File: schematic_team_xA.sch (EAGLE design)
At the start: 13 parts, among them U1 ATMEGA328P-AU

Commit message: Deleted copies
Deleted copies from the original location of the library files
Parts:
- removed R5, R6: (no value), resistor:R-US_R0402
- added R_VD1, R_VD2: 100kΩ, rcl:R-US_R0603
- C1: value (none) -> 100μF
- R_LED1, R_LED2, R_LED3, R_LED4: value (none) -> 150Ω
- renumbered R1 to R_LED1, R2 to R_LED2, R3 to R_LED3, R4 to R_LED4
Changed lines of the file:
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@@
 <part name="U1" library="ATMEGA328P-AU" deviceset="ATMEGA328P-AU" device=""/>
 <part name="U$1" library="nrf24l01" deviceset="NRF24L01" device=""/>
-<part name="R1" library="rcl" deviceset="R-US_" device="R0603"/>
-<part name="R2" library="rcl" deviceset="R-US_" device="R0603"/>
-<part name="R3" library="rcl" deviceset="R-US_" device="R0603"/>
-<part name="R4" library="rcl" deviceset="R-US_" device="R0603"/>
+<part name="R_LED1" library="rcl" deviceset="R-US_" device="R0603" value="150Ω"/>
+<part name="R_LED2" library="rcl" deviceset="R-US_" device="R0603" value="150Ω"/>
+<part name="R_LED3" library="rcl" deviceset="R-US_" device="R0603" value="150Ω"/>
+<part name="R_LED4" library="rcl" deviceset="R-US_" device="R0603" value="150Ω"/>
 <part name="D1" library="LEDs" deviceset="LED-RED" device="0603" value="RED"/>
 <part name="D2" library="LEDs" deviceset="LED-GREEN" device="0603" value="GREEN"/>
 <part name="D3" library="LEDs" deviceset="LED-GREEN" device="0603" value="GREEN"/>
 <part name="D4" library="LEDs" deviceset="LED-RED" device="0603" value="RED"/>
-<part name="C1" library="resistor" library_urn="urn:adsk.eagle:library:348" deviceset="C-US" device="C0805" package3d_urn="urn:adsk.eagle:package:26137/1"/>
-<part name="R5" library="resistor" deviceset="R-US_" device="R0402"/>
-<part name="R6" library="resistor" deviceset="R-US_" device="R0402"/>
+<part name="C1" library="resistor" library_urn="urn:adsk.eagle:library:348" deviceset="C-US" device="C0805" package3d_urn="urn:adsk.eagle:package:26137/1" value="100μF"/>
+<part name="R_VD1" library="rcl" deviceset="R-US_" device="R0603" value="100kΩ"/>
+<part name="R_VD2" library="rcl" deviceset="R-US_" device="R0603" value="100kΩ"/>
 </parts>
 <sheets>
@@
 <instance part="U1" gate="A" x="12.7" y="50.8"/>
 <instance part="U$1" gate="G$1" x="-7.62" y="58.42"/>
-<instance part="R1" gate="G$1" x="25.4" y="81.28"/>
-<instance part="R2" gate="G$1" x="25.4" y="73.66"/>
-<instance part="R3" gate="G$1" x="40.64" y="81.28"/>
-<instance part="R4" gate="G$1" x="40.64" y="73.66"/>
+<instance part="R_LED1" gate="G$1" x="25.4" y="81.28"/>
+<instance part="R_LED2" gate="G$1" x="25.4" y="73.66"/>
+<instance part="R_LED3" gate="G$1" x="40.64" y="81.28"/>
+<instance part="R_LED4" gate="G$1" x="40.64" y="73.66"/>
 <instance part="D1" gate="G$1" x="68.58" y="81.28"/>
 <instance part="D2" gate="G$1" x="81.28" y="81.28"/>
@@
 <instance part="D4" gate="G$1" x="68.58" y="71.12"/>
 <instance part="C1" gate="G$1" x="93.98" y="81.28"/>
-<instance part="R5" gate="G$1" x="53.34" y="81.28"/>
-<instance part="R6" gate="G$1" x="53.34" y="73.66"/>
+<instance part="R_VD1" gate="G$1" x="53.34" y="81.28"/>
+<instance part="R_VD2" gate="G$1" x="53.34" y="73.66"/>
 </instances>
 <busses>

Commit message: Added parts
Added parts to schematic
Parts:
- added U$2: TI-LM2665M6, TI-LM2665M6:TI-LM2665M6
- added U2: MPU-6050, MPU-6050:MPU-6050
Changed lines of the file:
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@@
 <part name="R_VD1" library="rcl" deviceset="R-US_" device="R0603" value="100kΩ"/>
 <part name="R_VD2" library="rcl" deviceset="R-US_" device="R0603" value="100kΩ"/>
+<part name="U$2" library="TI-LM2665M6" deviceset="TI-LM2665" device="M6"/>
+<part name="U2" library="MPU-6050" deviceset="MPU-6050" device=""/>
 </parts>
 <sheets>
@@
 <instance part="R_VD1" gate="G$1" x="53.34" y="81.28"/>
 <instance part="R_VD2" gate="G$1" x="53.34" y="73.66"/>
+<instance part="U$2" gate="G$1" x="-12.7" y="15.24"/>
+<instance part="U2" gate="G$1" x="132.08" y="78.74"/>
 </instances>
 <busses>

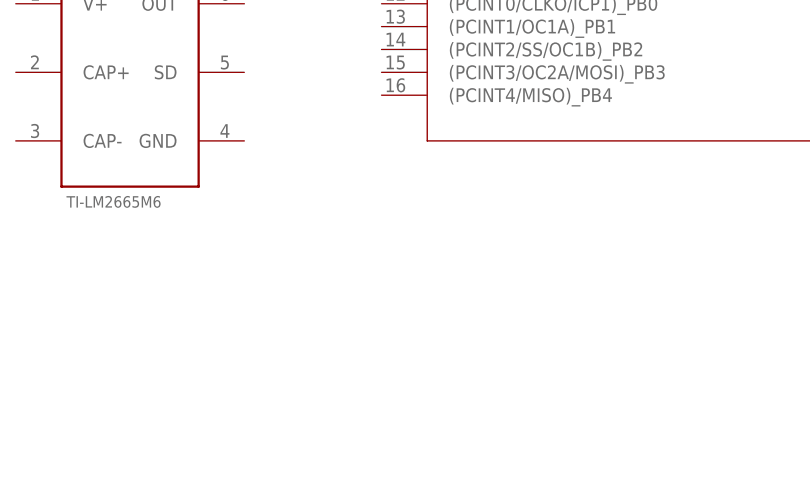
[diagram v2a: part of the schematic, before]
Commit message: NMOS Library
Created the NMOS library w/Rob and added it to the schematic
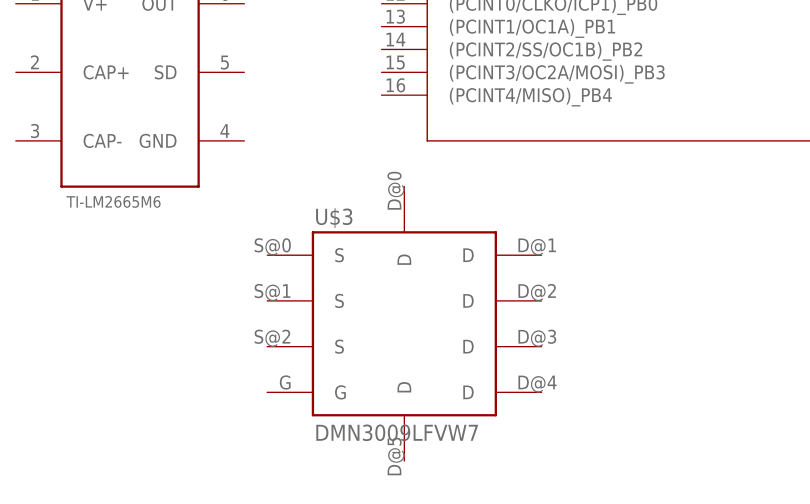
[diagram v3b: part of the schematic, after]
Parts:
- added U$3: DMN3009LFVW7, DMN3009LFVW:DMN3009LFVW7
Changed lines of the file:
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@@
 <part name="U$2" library="TI-LM2665M6" deviceset="TI-LM2665" device="M6"/>
 <part name="U2" library="MPU-6050" deviceset="MPU-6050" device=""/>
+<part name="U$3" library="DMN3009LFVW" deviceset="DMN3009LFVW" device="7"/>
 </parts>
 <sheets>
@@
 <instance part="U$2" gate="G$1" x="-12.7" y="15.24"/>
 <instance part="U2" gate="G$1" x="132.08" y="78.74"/>
+<instance part="U$3" gate="G$1" x="17.78" y="-12.7"/>
 </instances>
 <busses>

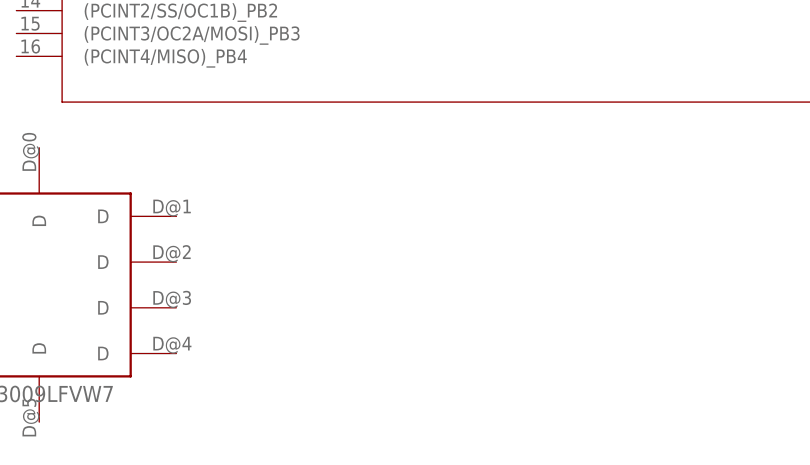
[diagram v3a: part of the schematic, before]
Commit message: Oscillator symbol/footprint
Created library file for our 16MHz oscillator and added it to the schematic
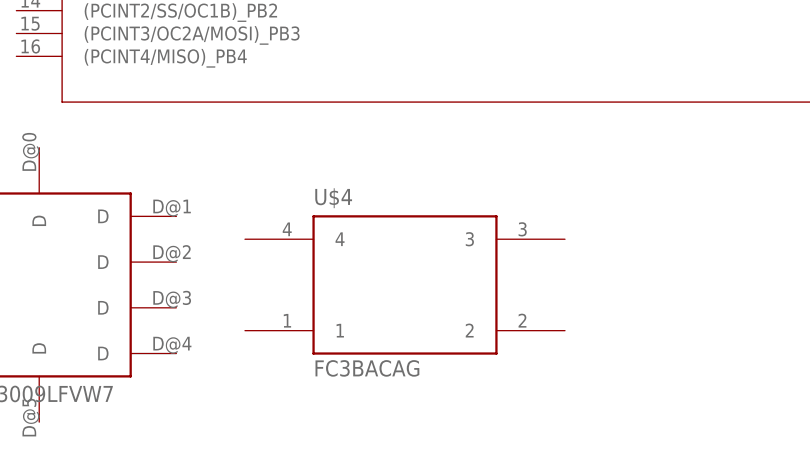
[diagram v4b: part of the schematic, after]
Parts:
- added U$4: FC3BACAG, FC3BACAG:FC3BACAG
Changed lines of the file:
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@@
 <part name="U2" library="MPU-6050" deviceset="MPU-6050" device=""/>
 <part name="U$3" library="DMN3009LFVW" deviceset="DMN3009LFVW" device="7"/>
+<part name="U$4" library="FC3BACAG" deviceset="FC3BACA" device="G"/>
 </parts>
 <sheets>
@@
 <instance part="U2" gate="G$1" x="132.08" y="78.74"/>
 <instance part="U$3" gate="G$1" x="17.78" y="-12.7"/>
+<instance part="U$4" gate="G$1" x="58.42" y="-12.7"/>
 </instances>
 <busses>

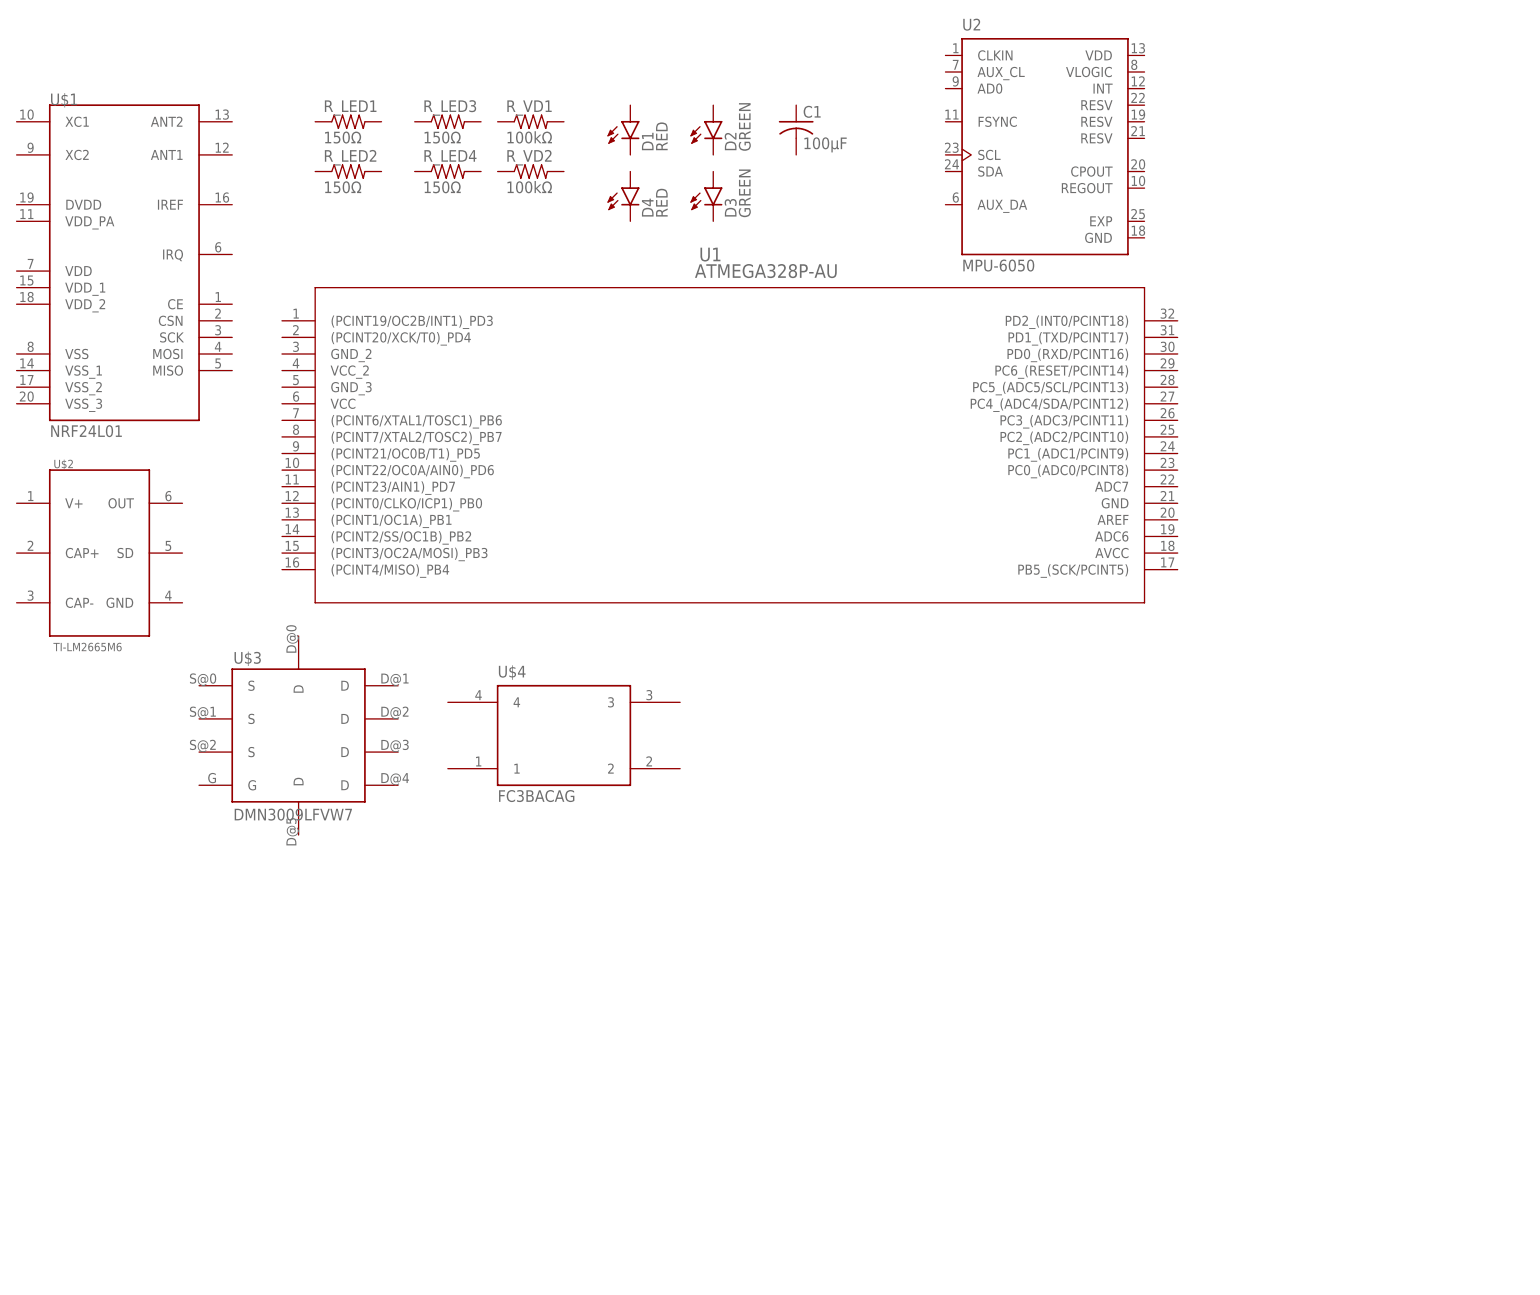
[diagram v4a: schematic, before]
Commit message: Crystal Circuit
Wired the crystal on the board layout and adjusted the lbr file
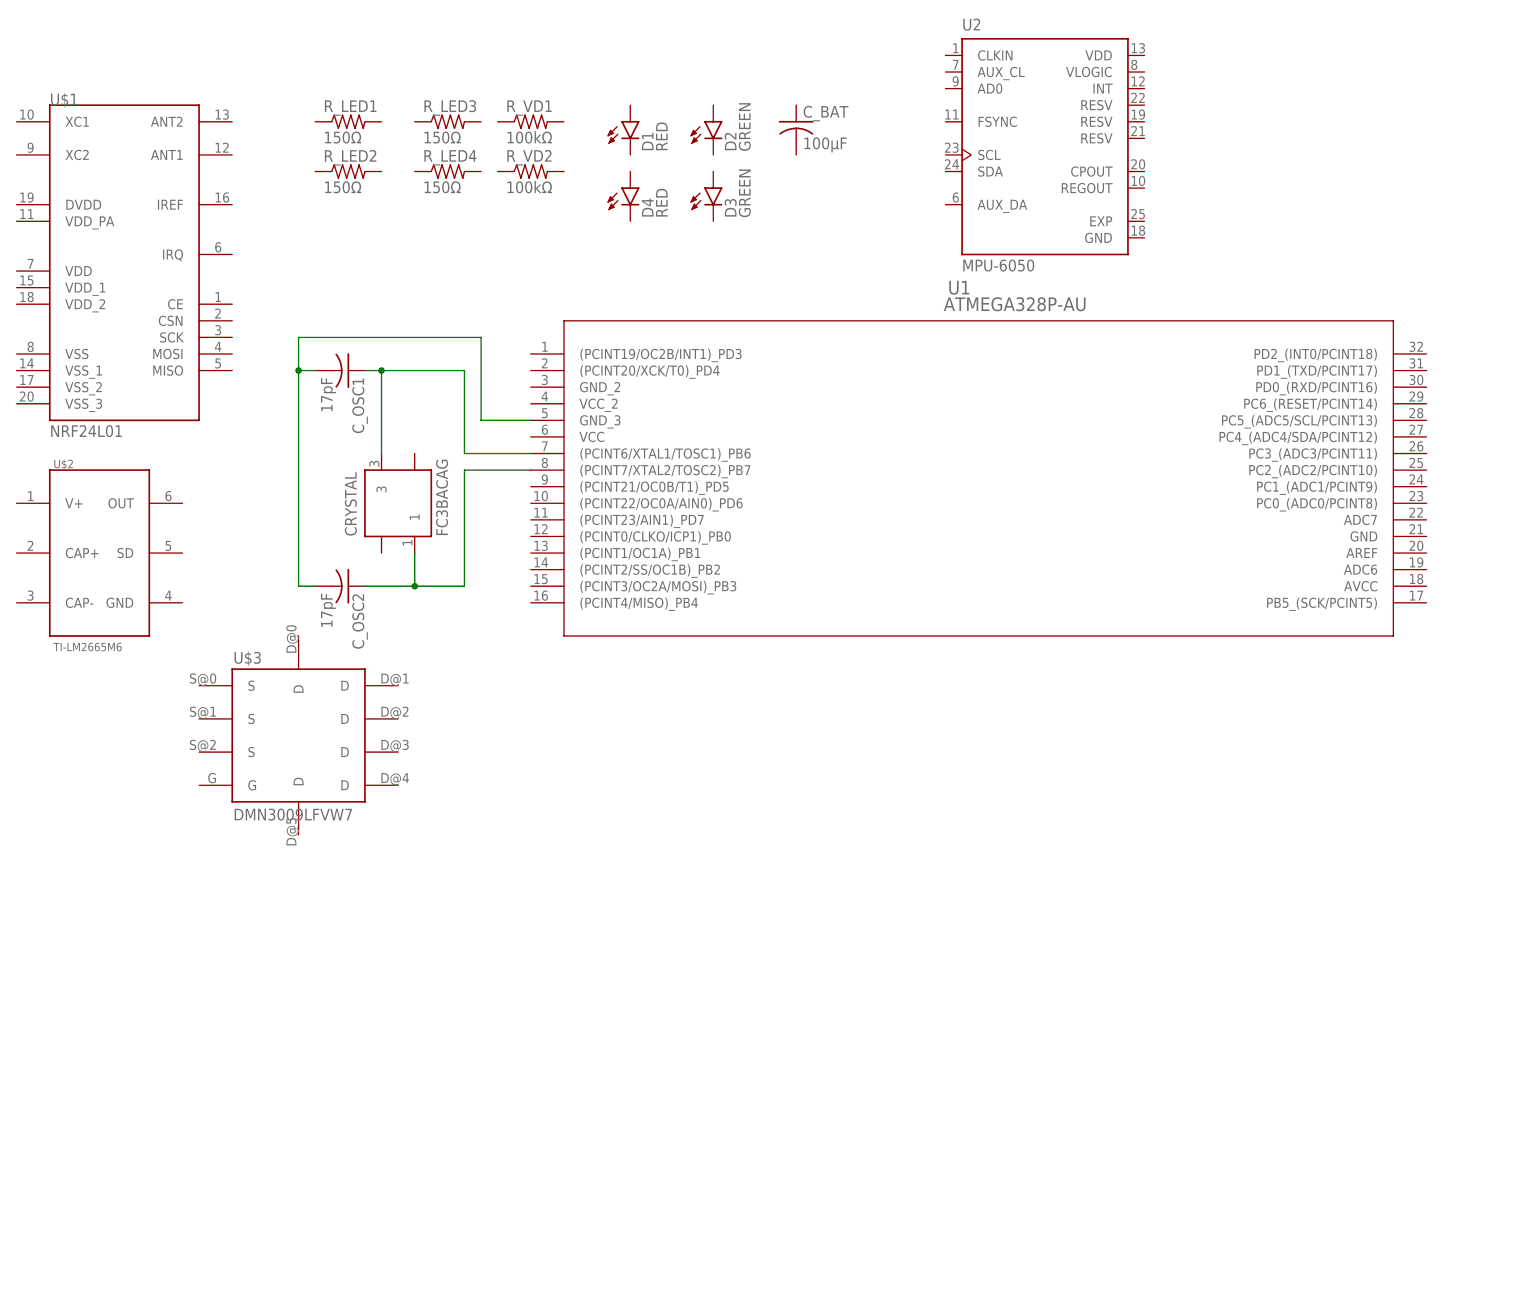
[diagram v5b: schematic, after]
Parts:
- removed U$4: FC3BACAG, FC3BACAG:FC3BACAG
- added CRYSTAL: FC3BACAG, FC3BACAG:FC3BACAG
- added C_OSC1, C_OSC2: 17pF, resistor:C-USC0805
- renumbered C1 to C_BAT
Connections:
- new net N$1: CRYSTAL.3, C_OSC1.1, U1.(PCINT6/XTAL1/TOSC1)_PB6
- new net N$2: CRYSTAL.1, C_OSC2.1, U1.(PCINT7/XTAL2/TOSC2)_PB7
- new net N$3: C_OSC1.2, C_OSC2.2, U1.GND_3
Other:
- moved on the sheet: U1
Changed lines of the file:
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@@
 <part name="D3" library="LEDs" deviceset="LED-GREEN" device="0603" value="GREEN"/>
 <part name="D4" library="LEDs" deviceset="LED-RED" device="0603" value="RED"/>
-<part name="C1" library="resistor" library_urn="urn:adsk.eagle:library:348" deviceset="C-US" device="C0805" package3d_urn="urn:adsk.eagle:package:26137/1" value="100μF"/>
+<part name="C_BAT" library="resistor" library_urn="urn:adsk.eagle:library:348" deviceset="C-US" device="C0805" package3d_urn="urn:adsk.eagle:package:26137/1" value="100μF"/>
 <part name="R_VD1" library="rcl" deviceset="R-US_" device="R0603" value="100kΩ"/>
 <part name="R_VD2" library="rcl" deviceset="R-US_" device="R0603" value="100kΩ"/>
@@
 <part name="U2" library="MPU-6050" deviceset="MPU-6050" device=""/>
 <part name="U$3" library="DMN3009LFVW" deviceset="DMN3009LFVW" device="7"/>
-<part name="U$4" library="FC3BACAG" deviceset="FC3BACA" device="G"/>
+<part name="C_OSC1" library="resistor" library_urn="urn:adsk.eagle:library:348" deviceset="C-US" device="C0805" package3d_urn="urn:adsk.eagle:package:26137/1" value="17pF"/>
+<part name="C_OSC2" library="resistor" library_urn="urn:adsk.eagle:library:348" deviceset="C-US" device="C0805" package3d_urn="urn:adsk.eagle:package:26137/1" value="17pF"/>
+<part name="CRYSTAL" library="FC3BACAG" deviceset="FC3BACA" device="G"/>
 </parts>
 <sheets>
@@
 </plain>
 <instances>
-<instance part="U1" gate="A" x="12.7" y="50.8"/>
+<instance part="U1" gate="A" x="50.8" y="45.72"/>
 <instance part="U$1" gate="G$1" x="-7.62" y="58.42"/>
 <instance part="R_LED1" gate="G$1" x="25.4" y="81.28"/>
@@
 <instance part="D3" gate="G$1" x="81.28" y="71.12"/>
 <instance part="D4" gate="G$1" x="68.58" y="71.12"/>
-<instance part="C1" gate="G$1" x="93.98" y="81.28"/>
+<instance part="C_BAT" gate="G$1" x="93.98" y="81.28"/>
 <instance part="R_VD1" gate="G$1" x="53.34" y="81.28"/>
 <instance part="R_VD2" gate="G$1" x="53.34" y="73.66"/>
@@
 <instance part="U2" gate="G$1" x="132.08" y="78.74"/>
 <instance part="U$3" gate="G$1" x="17.78" y="-12.7"/>
-<instance part="U$4" gate="G$1" x="58.42" y="-12.7"/>
+<instance part="C_OSC1" gate="G$1" x="25.4" y="43.18" rot="R270"/>
+<instance part="C_OSC2" gate="G$1" x="25.4" y="10.16" rot="R270"/>
+<instance part="CRYSTAL" gate="G$1" x="33.02" y="22.86" rot="R90"/>
 </instances>
 <busses>
 </busses>
 <nets>
+<net name="N$1" class="0">
+<segment>
+<pinref part="U1" gate="A" pin="(PCINT6/XTAL1/TOSC1)_PB6"/>
+<wire x1="53.34" y1="30.48" x2="43.18" y2="30.48" width="0.1524" layer="91"/>
+<wire x1="43.18" y1="30.48" x2="43.18" y2="43.18" width="0.1524" layer="91"/>
+<wire x1="43.18" y1="43.18" x2="30.48" y2="43.18" width="0.1524" layer="91"/>
+<wire x1="30.48" y1="30.48" x2="30.48" y2="43.18" width="0.1524" layer="91"/>
+<pinref part="C_OSC1" gate="G$1" pin="1"/>
+<wire x1="30.48" y1="43.18" x2="27.94" y2="43.18" width="0.1524" layer="91"/>
+<junction x="30.48" y="43.18"/>
+<pinref part="CRYSTAL" gate="G$1" pin="3"/>
+</segment>
+</net>
+<net name="N$2" class="0">
+<segment>
+<pinref part="U1" gate="A" pin="(PCINT7/XTAL2/TOSC2)_PB7"/>
+<wire x1="53.34" y1="27.94" x2="43.18" y2="27.94" width="0.1524" layer="91"/>
+<wire x1="43.18" y1="27.94" x2="43.18" y2="10.16" width="0.1524" layer="91"/>
+<pinref part="C_OSC2" gate="G$1" pin="1"/>
+<wire x1="43.18" y1="10.16" x2="35.56" y2="10.16" width="0.1524" layer="91"/>
+<wire x1="35.56" y1="10.16" x2="27.94" y2="10.16" width="0.1524" layer="91"/>
+<wire x1="35.56" y1="15.24" x2="35.56" y2="10.16" width="0.1524" layer="91"/>
+<junction x="35.56" y="10.16"/>
+<pinref part="CRYSTAL" gate="G$1" pin="1"/>
+</segment>
+</net>
+<net name="N$3" class="0">
+<segment>
+<pinref part="C_OSC2" gate="G$1" pin="2"/>
+<wire x1="20.32" y1="10.16" x2="17.78" y2="10.16" width="0.1524" layer="91"/>
+<wire x1="17.78" y1="10.16" x2="17.78" y2="43.18" width="0.1524" layer="91"/>
+<wire x1="17.78" y1="43.18" x2="17.78" y2="48.26" width="0.1524" layer="91"/>
+<wire x1="17.78" y1="48.26" x2="45.72" y2="48.26" width="0.1524" layer="91"/>
+<wire x1="45.72" y1="48.26" x2="45.72" y2="35.56" width="0.1524" layer="91"/>
+<pinref part="U1" gate="A" pin="GND_3"/>
+<wire x1="45.72" y1="35.56" x2="53.34" y2="35.56" width="0.1524" layer="91"/>
+<pinref part="C_OSC1" gate="G$1" pin="2"/>
+<wire x1="20.32" y1="43.18" x2="17.78" y2="43.18" width="0.1524" layer="91"/>
+<junction x="17.78" y="43.18"/>
+</segment>
+</net>
 </nets>
 </sheet>
